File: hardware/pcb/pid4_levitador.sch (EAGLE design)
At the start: 128 parts, among them P1_C1 1u, P1_C2 1u, P1_J_IN VSENSOR, P1_J_OUT VPID, P1_J_PWR PWR, P1_POT1 22k, P1_POT2 220k, P1_POT3 22k, P1_R1 10k, P1_R10 1k, P1_R11 1M, P1_R12 160k, P1_R13 240k, P1_R14 96k, P1_R15 160k, P1_R2 10k, P1_R3 10k, P1_R4 10k, P1_R5 10k, P1_R6 1k, P1_R7 10k, P1_R8 10k, P1_R9 10k, P1_RBIAS 4.4k, P1_ROFFSET 10k, P1_U1 LM741, P1_U2 LM741, P1_U3 LM741, P1_U4 LM741, P1_U5 LM741, P1_U6 LM741, P1_U7 LM741, P2_C1 1u, P2_C2 1u, P2_J_IN VSENSOR, P2_J_OUT VPID, P2_J_PWR PWR, P2_POT1 22k, P2_POT2 220k, P2_POT3 22k, P2_R1 10k, P2_R10 1k, P2_R11 1M, P2_R12 160k, P2_R13 240k, P2_R14 96k, P2_R15 160k, P2_R2 10k, P2_R3 10k, P2_R4 10k, P2_R5 10k, P2_R6 1k, P2_R7 10k, P2_R8 10k, P2_R9 10k, P2_RBIAS 4.4k, P2_ROFFSET 10k, P2_U1 LM741, P2_U2 LM741, P2_U3 LM741, P2_U4 LM741, P2_U5 LM741, P2_U6 LM741, P2_U7 LM741, P3_C1 1u, P3_C2 1u, P3_J_IN VSENSOR, P3_J_OUT VPID, P3_J_PWR PWR, P3_POT1 22k, P3_POT2 220k, P3_POT3 22k, P3_R1 10k, P3_R10 1k, P3_R11 1M, P3_R12 160k, P3_R13 240k, P3_R14 96k, P3_R15 160k, P3_R2 10k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

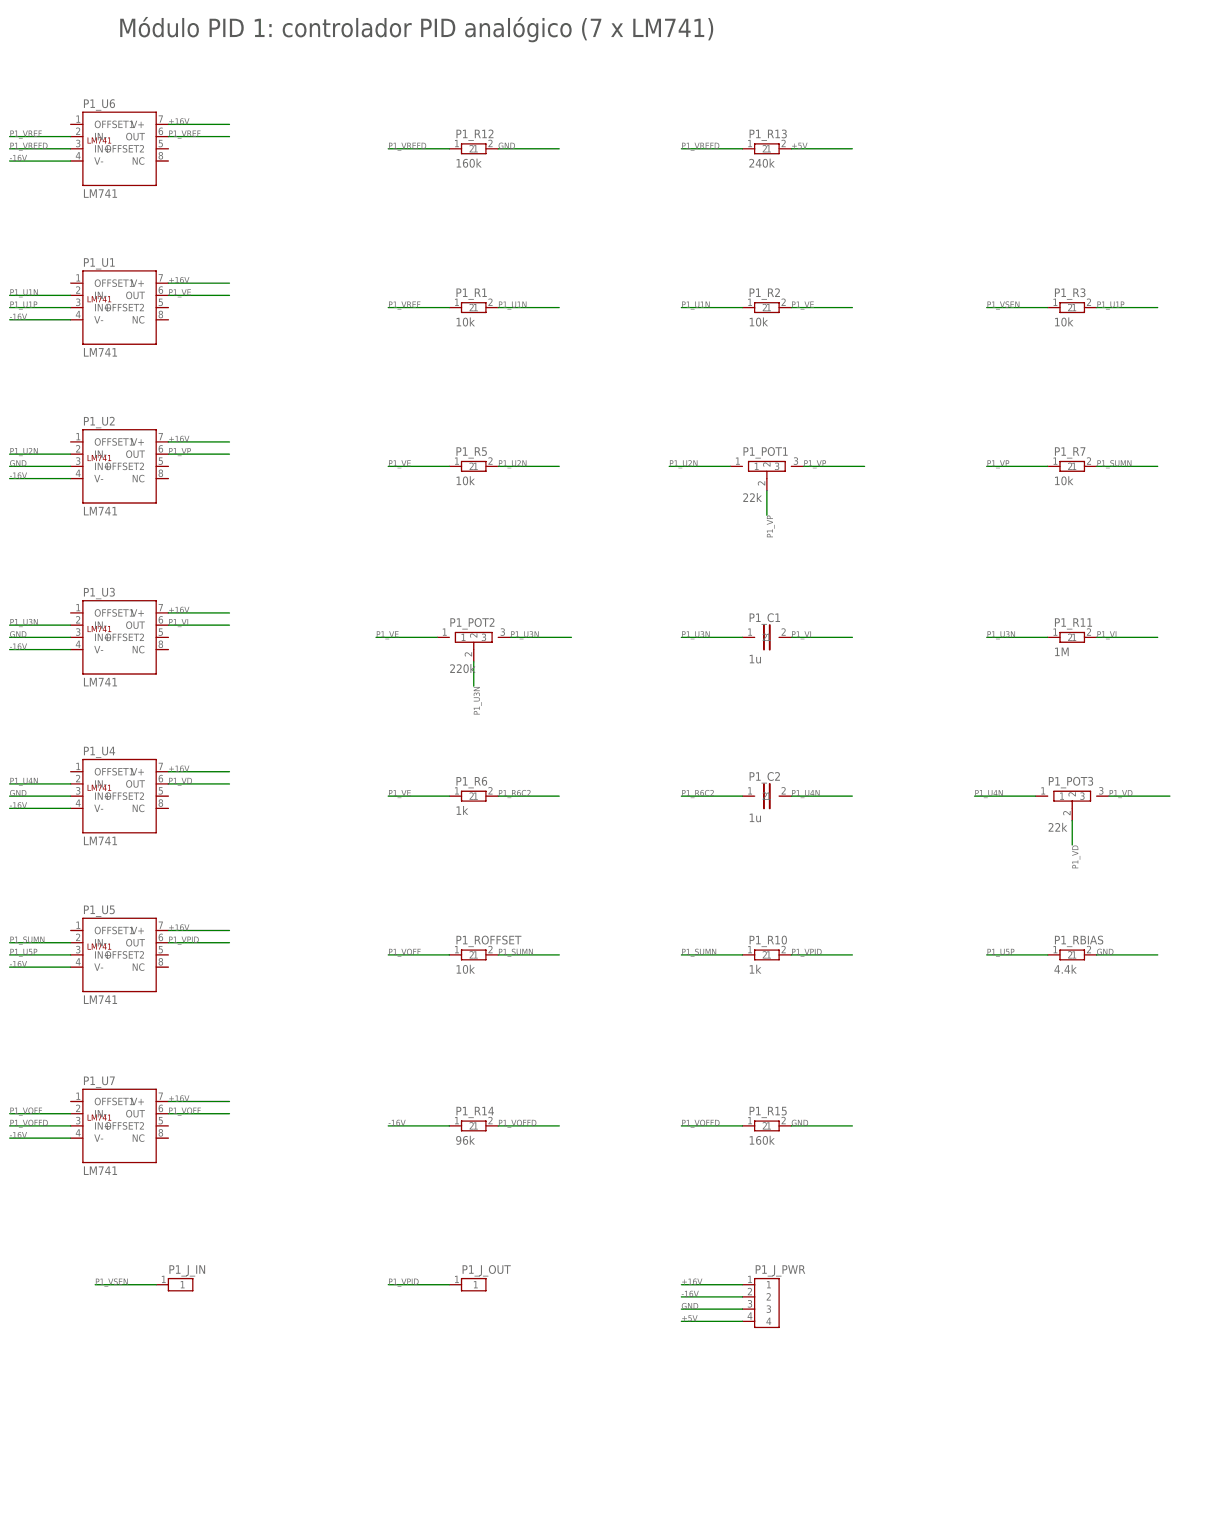
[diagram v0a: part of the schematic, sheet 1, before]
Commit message: Rehace la placa de 4 PID con TL074CN (2 por controlador, DIP-14) en lugar de LM741
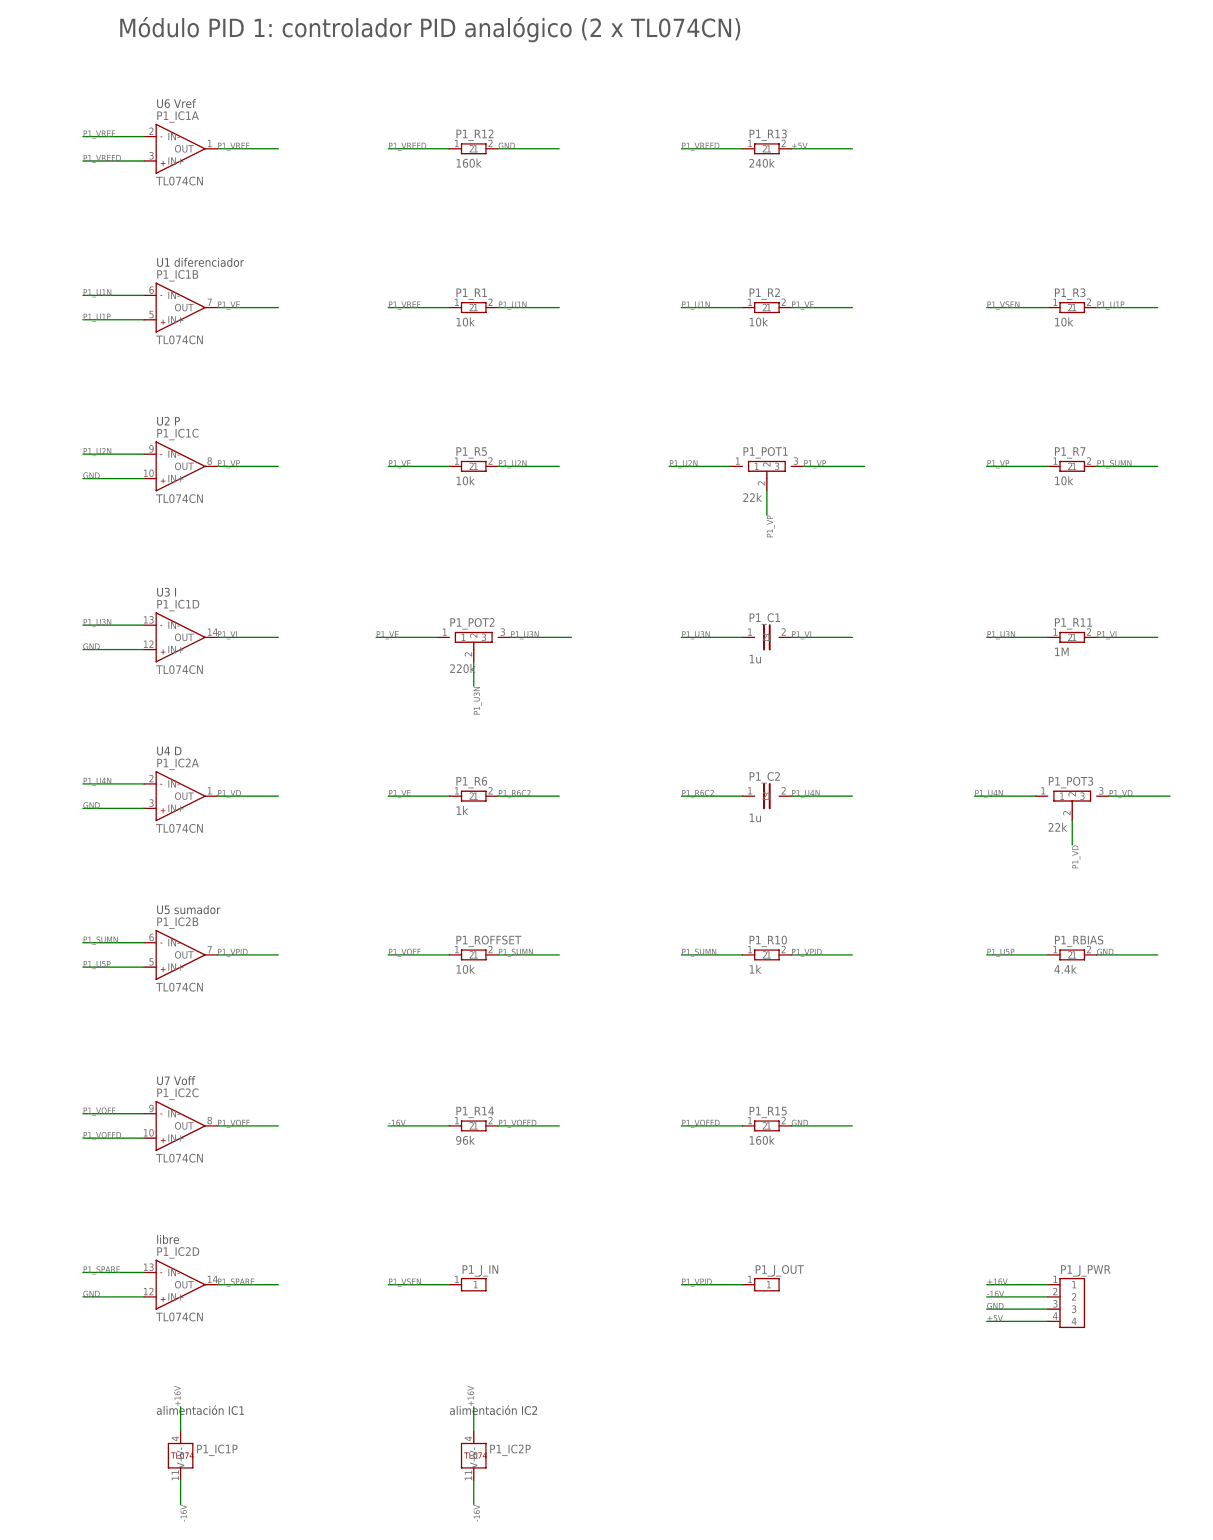
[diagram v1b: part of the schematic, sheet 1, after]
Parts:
- removed P1_U1, P1_U2, P1_U3, P1_U4, P1_U5, P1_U6, P1_U7, P2_U1, P2_U2, P2_U3, P2_U4, P2_U5, P2_U6, P2_U7, P3_U1, P3_U2, P3_U3, P3_U4, P3_U5, P3_U6, P3_U7, P4_U1, P4_U2, P4_U3, P4_U4, P4_U5, P4_U6, P4_U7: LM741, pid4:LM741
- added P1_IC1, P1_IC2, P2_IC1, P2_IC2, P3_IC1, P3_IC2, P4_IC1, P4_IC2: TL074CN, pid4:TL074
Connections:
- new net P1_SPARE: P1_IC2D.IN-, P1_IC2D.OUT
- new net P2_SPARE: P2_IC2D.IN-, P2_IC2D.OUT
- new net P3_SPARE: P3_IC2D.IN-, P3_IC2D.OUT
- new net P4_SPARE: P4_IC2D.IN-, P4_IC2D.OUT
- net +16V: now also P1_IC1P.V+, P1_IC2P.V+, P2_IC1P.V+, P2_IC2P.V+, P3_IC1P.V+, P3_IC2P.V+, P4_IC1P.V+, P4_IC2P.V+; no longer P1_U1.V+, P1_U2.V+, P1_U3.V+, P1_U4.V+, P1_U5.V+, P1_U6.V+, P1_U7.V+, P2_U1.V+, P2_U2.V+, P2_U3.V+, P2_U4.V+, P2_U5.V+, P2_U6.V+, P2_U7.V+, P3_U1.V+, P3_U2.V+, P3_U3.V+, P3_U4.V+, P3_U5.V+, P3_U6.V+, P3_U7.V+, P4_U1.V+, P4_U2.V+, P4_U3.V+, P4_U4.V+, P4_U5.V+, P4_U6.V+, P4_U7.V+
- net -16V: now also P1_IC1P.V-, P1_IC2P.V-, P2_IC1P.V-, P2_IC2P.V-, P3_IC1P.V-, P3_IC2P.V-, P4_IC1P.V-, P4_IC2P.V-; no longer P1_U1.V-, P1_U2.V-, P1_U3.V-, P1_U4.V-, P1_U5.V-, P1_U6.V-, P1_U7.V-, P2_U1.V-, P2_U2.V-, P2_U3.V-, P2_U4.V-, P2_U5.V-, P2_U6.V-, P2_U7.V-, P3_U1.V-, P3_U2.V-, P3_U3.V-, P3_U4.V-, P3_U5.V-, P3_U6.V-, P3_U7.V-, P4_U1.V-, P4_U2.V-, P4_U3.V-, P4_U4.V-, P4_U5.V-, P4_U6.V-, P4_U7.V-
- net GND: now also P1_IC1C.IN+, P1_IC1D.IN+, P1_IC2A.IN+, P1_IC2D.IN+, P2_IC1C.IN+, P2_IC1D.IN+, P2_IC2A.IN+, P2_IC2D.IN+, P3_IC1C.IN+, P3_IC1D.IN+, P3_IC2A.IN+, P3_IC2D.IN+, P4_IC1C.IN+, P4_IC1D.IN+, P4_IC2A.IN+, P4_IC2D.IN+; no longer P1_U2.IN+, P1_U3.IN+, P1_U4.IN+, P2_U2.IN+, P2_U3.IN+, P2_U4.IN+, P3_U2.IN+, P3_U3.IN+, P3_U4.IN+, P4_U2.IN+, P4_U3.IN+, P4_U4.IN+
- net P1_SUMN: now also P1_IC2B.IN-; no longer P1_U5.IN-
- net P1_U1N: now also P1_IC1B.IN-; no longer P1_U1.IN-
- net P1_U1P: now also P1_IC1B.IN+; no longer P1_U1.IN+
- net P1_U2N: now also P1_IC1C.IN-; no longer P1_U2.IN-
- net P1_U3N: now also P1_IC1D.IN-; no longer P1_U3.IN-
- net P1_U4N: now also P1_IC2A.IN-; no longer P1_U4.IN-
- net P1_U5P: now also P1_IC2B.IN+; no longer P1_U5.IN+
- net P1_VD: now also P1_IC2A.OUT; no longer P1_U4.OUT
- net P1_VE: now also P1_IC1B.OUT; no longer P1_U1.OUT
- net P1_VI: now also P1_IC1D.OUT; no longer P1_U3.OUT
- net P1_VOFF: now also P1_IC2C.IN-, P1_IC2C.OUT; no longer P1_U7.IN-, P1_U7.OUT
- net P1_VOFFD: now also P1_IC2C.IN+; no longer P1_U7.IN+
- net P1_VP: now also P1_IC1C.OUT; no longer P1_U2.OUT
- net P1_VPID: now also P1_IC2B.OUT; no longer P1_U5.OUT
- net P1_VREF: now also P1_IC1A.IN-, P1_IC1A.OUT; no longer P1_U6.IN-, P1_U6.OUT
- net P1_VREFD: now also P1_IC1A.IN+; no longer P1_U6.IN+
- net P2_SUMN: now also P2_IC2B.IN-; no longer P2_U5.IN-
- net P2_U1N: now also P2_IC1B.IN-; no longer P2_U1.IN-
- net P2_U1P: now also P2_IC1B.IN+; no longer P2_U1.IN+
- net P2_U2N: now also P2_IC1C.IN-; no longer P2_U2.IN-
- net P2_U3N: now also P2_IC1D.IN-; no longer P2_U3.IN-
- net P2_U4N: now also P2_IC2A.IN-; no longer P2_U4.IN-
- net P2_U5P: now also P2_IC2B.IN+; no longer P2_U5.IN+
- net P2_VD: now also P2_IC2A.OUT; no longer P2_U4.OUT
- net P2_VE: now also P2_IC1B.OUT; no longer P2_U1.OUT
- net P2_VI: now also P2_IC1D.OUT; no longer P2_U3.OUT
- net P2_VOFF: now also P2_IC2C.IN-, P2_IC2C.OUT; no longer P2_U7.IN-, P2_U7.OUT
- net P2_VOFFD: now also P2_IC2C.IN+; no longer P2_U7.IN+
- net P2_VP: now also P2_IC1C.OUT; no longer P2_U2.OUT
- net P2_VPID: now also P2_IC2B.OUT; no longer P2_U5.OUT
- net P2_VREF: now also P2_IC1A.IN-, P2_IC1A.OUT; no longer P2_U6.IN-, P2_U6.OUT
- net P2_VREFD: now also P2_IC1A.IN+; no longer P2_U6.IN+
- net P3_SUMN: now also P3_IC2B.IN-; no longer P3_U5.IN-
- net P3_U1N: now also P3_IC1B.IN-; no longer P3_U1.IN-
- net P3_U1P: now also P3_IC1B.IN+; no longer P3_U1.IN+
- net P3_U2N: now also P3_IC1C.IN-; no longer P3_U2.IN-
- net P3_U3N: now also P3_IC1D.IN-; no longer P3_U3.IN-
- net P3_U4N: now also P3_IC2A.IN-; no longer P3_U4.IN-
- net P3_U5P: now also P3_IC2B.IN+; no longer P3_U5.IN+
- net P3_VD: now also P3_IC2A.OUT; no longer P3_U4.OUT
- net P3_VE: now also P3_IC1B.OUT; no longer P3_U1.OUT
- net P3_VI: now also P3_IC1D.OUT; no longer P3_U3.OUT
- net P3_VOFF: now also P3_IC2C.IN-, P3_IC2C.OUT; no longer P3_U7.IN-, P3_U7.OUT
- net P3_VOFFD: now also P3_IC2C.IN+; no longer P3_U7.IN+
- net P3_VP: now also P3_IC1C.OUT; no longer P3_U2.OUT
- net P3_VPID: now also P3_IC2B.OUT; no longer P3_U5.OUT
- net P3_VREF: now also P3_IC1A.IN-, P3_IC1A.OUT; no longer P3_U6.IN-, P3_U6.OUT
- net P3_VREFD: now also P3_IC1A.IN+; no longer P3_U6.IN+
- net P4_SUMN: now also P4_IC2B.IN-; no longer P4_U5.IN-
- net P4_U1N: now also P4_IC1B.IN-; no longer P4_U1.IN-
- net P4_U1P: now also P4_IC1B.IN+; no longer P4_U1.IN+
- net P4_U2N: now also P4_IC1C.IN-; no longer P4_U2.IN-
- net P4_U3N: now also P4_IC1D.IN-; no longer P4_U3.IN-
- net P4_U4N: now also P4_IC2A.IN-; no longer P4_U4.IN-
- net P4_U5P: now also P4_IC2B.IN+; no longer P4_U5.IN+
- net P4_VD: now also P4_IC2A.OUT; no longer P4_U4.OUT
- net P4_VE: now also P4_IC1B.OUT; no longer P4_U1.OUT
- net P4_VI: now also P4_IC1D.OUT; no longer P4_U3.OUT
- net P4_VOFF: now also P4_IC2C.IN-, P4_IC2C.OUT; no longer P4_U7.IN-, P4_U7.OUT
- net P4_VOFFD: now also P4_IC2C.IN+; no longer P4_U7.IN+
- net P4_VP: now also P4_IC1C.OUT; no longer P4_U2.OUT
- net P4_VPID: now also P4_IC2B.OUT; no longer P4_U5.OUT
- net P4_VREF: now also P4_IC1A.IN-, P4_IC1A.OUT; no longer P4_U6.IN-, P4_U6.OUT
- net P4_VREFD: now also P4_IC1A.IN+; no longer P4_U6.IN+
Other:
- note added: "Módulo PID 1: controlador PID analógico (2 x TL074CN)"
- note added: "Módulo PID 2: controlador PID analógico (2 x TL074CN)"
- note added: "Módulo PID 3: controlador PID analógico (2 x TL074CN)"
- note added: "Módulo PID 4: controlador PID analógico (2 x TL074CN)"
- note added: "U1 diferenciador"
- note added: "U2 P"
- note added: "U3 I"
- note added: "U4 D"
- note added: "U5 sumador"
- note added: "U6 Vref"
- note added: "U7 Voff"
- note added: "alimentación IC1"
- note added: "alimentación IC2"
- note added: "libre"
- note removed: "Módulo PID 1: controlador PID analógico (7 x LM741)"
- note removed: "Módulo PID 2: controlador PID analógico (7 x LM741)"
- note removed: "Módulo PID 3: controlador PID analógico (7 x LM741)"
- note removed: "Módulo PID 4: controlador PID analógico (7 x LM741)"
- moved on the sheet: P1_J_IN, P1_J_OUT, P1_J_PWR, P2_J_IN, P2_J_OUT, P2_J_PWR, P3_J_IN, P3_J_OUT, P3_J_PWR, P4_J_IN, P4_J_OUT, P4_J_PWR
